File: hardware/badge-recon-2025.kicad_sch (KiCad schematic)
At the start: 72 parts, among them J3 Battery, J5 OLED, P1 USB_C_Plug_USB2.0, Q1 DMG3415U-7, SW1 SW_Push, SW2 SW_Push, SW3 ON, SW4 SOURCE MAG, SW5 SW_Push, SW6 SW_Push, SW7 RESET, SW8 SW_Push, U1 PN7150B0HN_C11002E-PN7150B0HN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, U2 RP2040, U3 AP2114H, U4 W25Q16JV, U5 TC4424, Y1 27.12Mhz, Y2 12Mhz

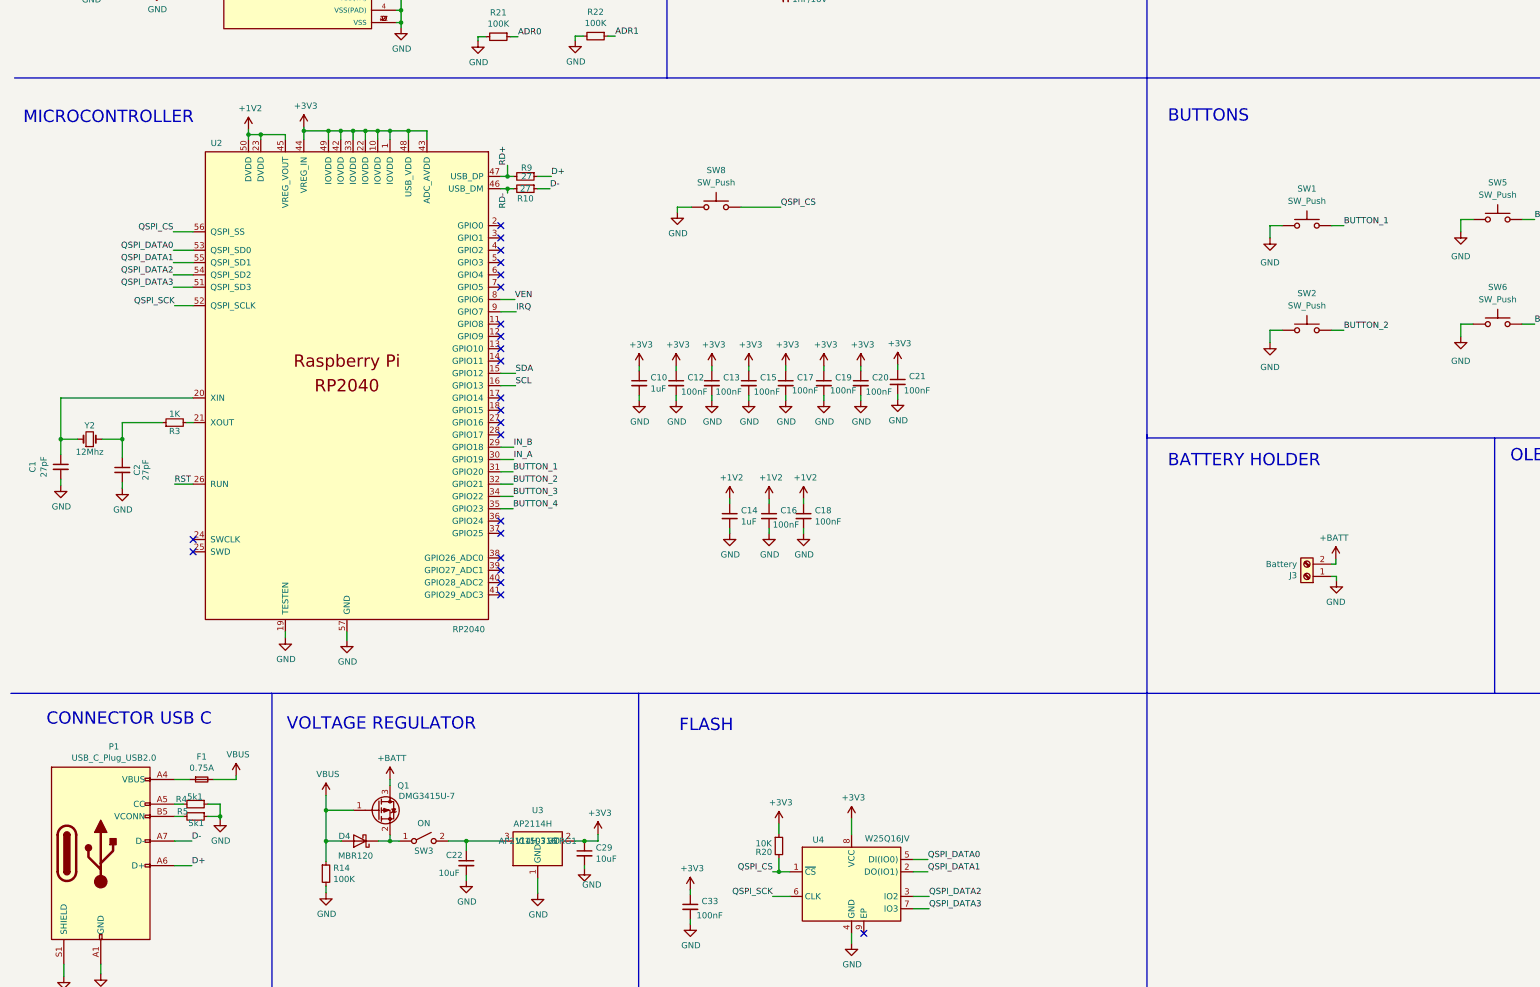
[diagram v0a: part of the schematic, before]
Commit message: feat(Hw): add expansor, 0 unconnected, missing pn7150 crystal
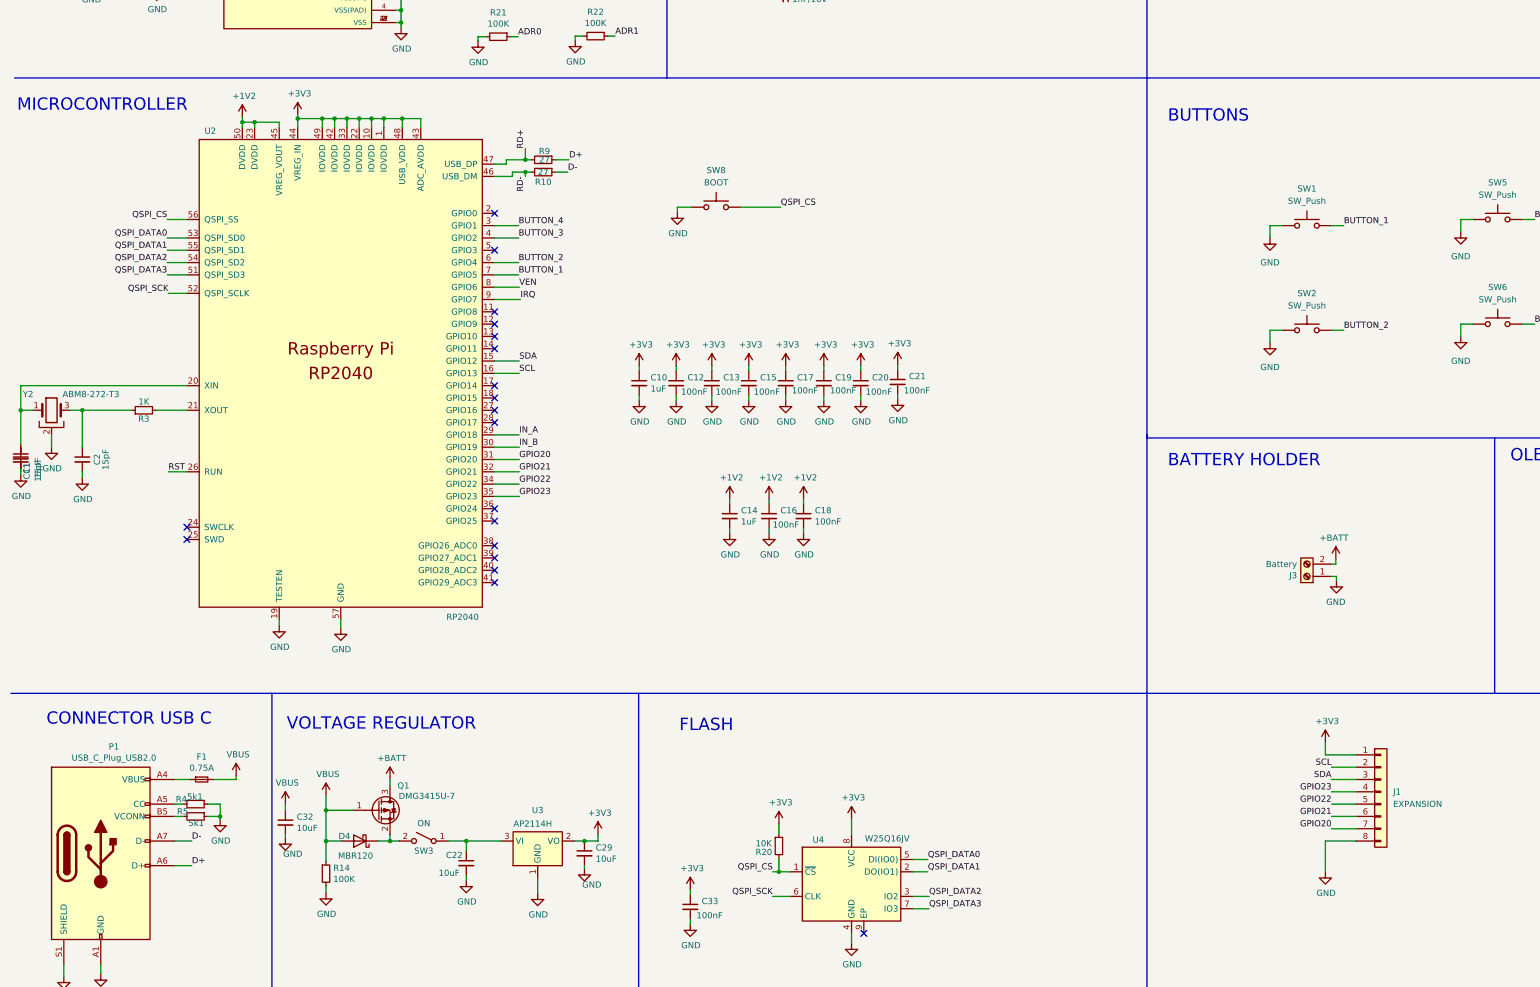
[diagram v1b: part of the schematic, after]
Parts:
- removed Y2: 12Mhz, Crystal:Crystal_SMD_5032-2Pin_5.0x3.2mm, symbol Device:Crystal_Small
- added C11: 15pF, Capacitor_SMD:C_0603_1608Metric, symbol Device:C_Small
- added C32: 10uF, Capacitor_SMD:C_0603_1608Metric, symbol Device:C_Small
- added J1: EXPANSION, Connector_PinHeader_2.54mm:PinHeader_1x08_P2.54mm_Vertical, symbol Connector_Generic:Conn_01x08
- added Y2: ABM8-272-T3, Crystal:Crystal_SMD_Abracon_ABM8G-4Pin_3.2x2.5mm, symbol Device:Crystal_GND2
- C1, C2: value 27pF -> 15pF; LCSC# C92670 -> C1644
- SW8: value SW_Push -> BOOT
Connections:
- net +3V3: now also J1.1 (Pin_1)
- net BUTTON_1: now also U2.7 (GPIO5); no longer U2.31 (GPIO20)
- net BUTTON_2: now also U2.6 (GPIO4); no longer U2.32 (GPIO21)
- net BUTTON_3: now also U2.4 (GPIO2); no longer U2.34 (GPIO22)
- net BUTTON_4: now also U2.3 (GPIO1); no longer U2.35 (GPIO23)
- net GND: now also C32.2, J1.8 (Pin_8), Y2.2
- net IN_A: now also U2.29 (GPIO18); no longer U2.30 (GPIO19)
- net IN_B: now also U2.30 (GPIO19); no longer U2.29 (GPIO18)
- net SCL: now also J1.2 (Pin_2)
- net SDA: now also J1.3 (Pin_3)
- net VBUS: now also C32.1
- net at C1.1, U2.20 (XIN): now also Y2.1
- net at C2.1, R3.1: now also Y2.3
- net at D4.1 (K), Q1.2 (S): now also SW3.2 (B); no longer SW3.1 (A)
- net at C22.1, U3.3 (VI): now also SW3.1 (A); no longer SW3.2 (B)
- new net GPIO20: J1.7 (Pin_7), U2.31 (GPIO20)
- new net GPIO21: J1.6 (Pin_6), U2.32 (GPIO21)
- new net GPIO22: J1.5 (Pin_5), U2.34 (GPIO22)
- new net GPIO23: J1.4 (Pin_4), U2.35 (GPIO23)
- no-connect marks 26 -> 22
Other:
- moved on the sheet: C1, C2, R10, R3, R9, U2

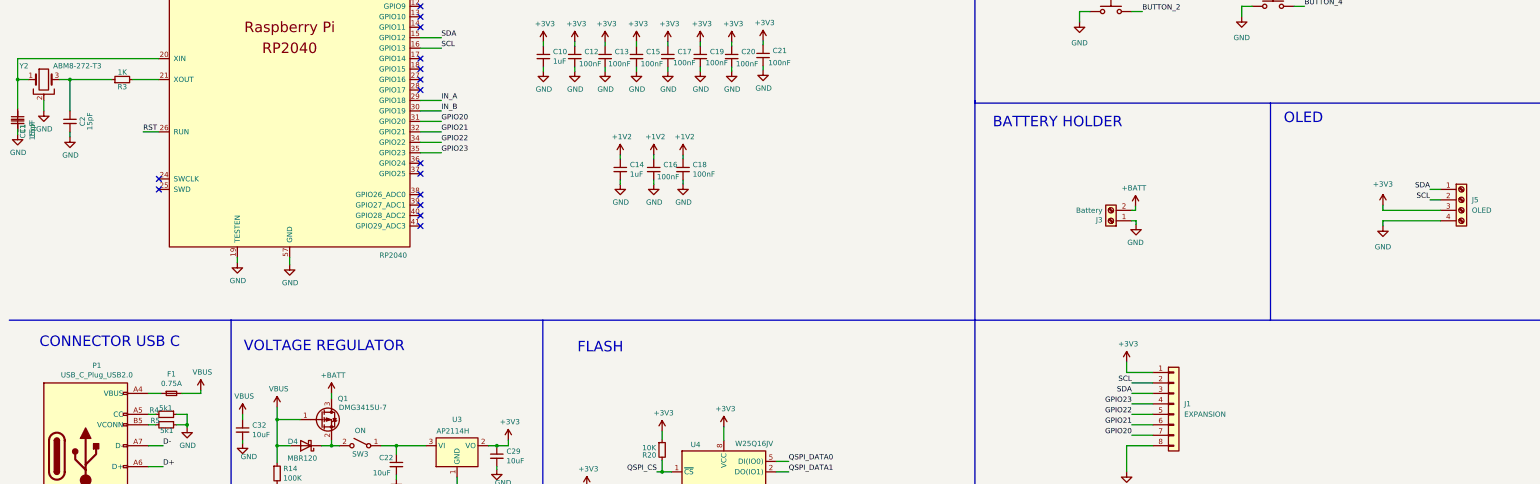
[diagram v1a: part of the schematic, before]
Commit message: feat(Hw): update part numbers for jlcpcb
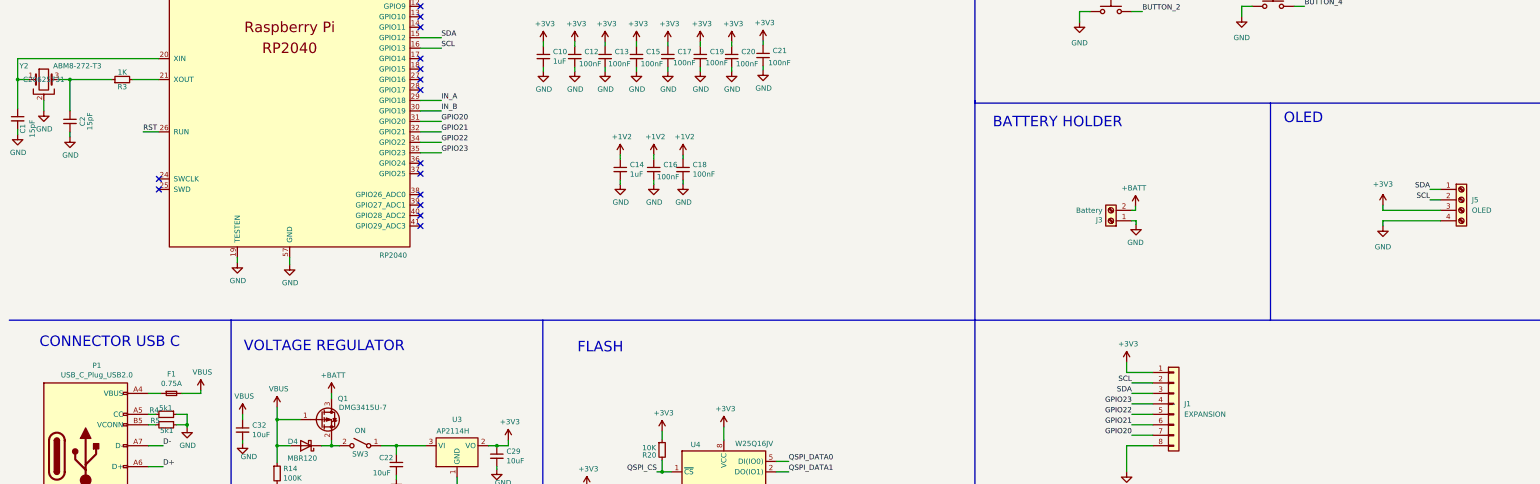
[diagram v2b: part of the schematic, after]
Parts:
- removed C11: 15pF, Capacitor_SMD:C_0603_1608Metric, symbol Device:C_Small
- J1, J5: LCSC# (none) -> -
- U5: manf# TC4424AVOA -> C7498963
- Y1: LCSC# C910048 -> C338245; manf# 520-271.2-6-37-JTNT -> XRCGB27M120F3M10R0
- Y2: LCSC# (none) -> C20625731
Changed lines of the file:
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@@
 			)
 		)
+		(property "LCSC#" "-"
+			(at 294.64 238.76 0)
+			(effects
+				(font
+					(size 1.27 1.27)
+				)
+			)
+		)
 		(pin "3"
 		)
@@
 			)
 		)
-		(property "manf#" "520-271.2-6-37-JTNT"
+		(property "manf#" "XRCGB27M120F3M10R0"
 			(at 28.575 63.627 0)
 			(effects
@@
 			)
 		)
-		(property "LCSC#" "C910048"
+		(property "LCSC#" "C338245"
 			(at 28.575 63.627 0)
 			(effects
@@
 			)
 		)
+		(property "LCSC#" "-"
+			(at 364.49 189.23 0)
+			(effects
+				(font
+					(size 1.27 1.27)
+				)
+			)
+		)
 		(pin "1"
 		)
@@
 			)
 		)
-		(property "manf#" "TC4424AVOA"
+		(property "manf#" "C7498963"
 			(at 327.787 45.339 0)
 			(effects
@@
 			)
 		)
+		(property "LCSC#" "C20625731 "
+			(at 20.32 160.02 0)
+			(effects
+				(font
+					(size 1.27 1.27)
+				)
+			)
+		)
 		(pin "1"
 		)
@@
 					(unit 1)
 				)
-			)
-		)
-	)
-	(symbol
-		(lib_id "Device:C_Small")
-		(at 13.97 170.18 0)
-		(unit 1)
-		(exclude_from_sim no)
-		(in_bom yes)
-		(on_board yes)
-		(dnp no)
-		(property "Reference" "C11"
-			(at 15.2146 172.593 90)
-			(effects
-				(font
-					(size 1.27 1.27)
-				)
-			)
-		)
-		(property "Value" "15pF"
-			(at 17.526 172.593 90)
-			(effects
-				(font
-					(size 1.27 1.27)
-				)
-			)
-		)
-		(property "Footprint" "Capacitor_SMD:C_0603_1608Metric"
-			(at 13.97 170.18 0)
-			(effects
-				(font
-					(size 1.27 1.27)
-				)
-				(hide yes)
-			)
-		)
-		(property "Datasheet" ""
-			(at 13.97 170.18 0)
-			(effects
-				(font
-					(size 1.27 1.27)
-				)
-				(hide yes)
-			)
-		)
-		(property "Description" ""
-			(at 13.97 170.18 0)
-			(effects
-				(font
-					(size 1.27 1.27)
-				)
-			)
-		)
-		(property "LCSC#" "C1644"
-			(at 13.97 170.18 0)
-			(effects
-				(font
-					(size 1.27 1.27)
-				)
-				(hide yes)
-			)
-		)
-		(property "manf#" ""
-			(at 13.97 170.18 0)
-			(effects
-				(font
-					(size 1.27 1.27)
-				)
-				(hide yes)
-			)
-		)
-		(property "provedor" "LCSC"
-			(at 13.97 170.18 0)
-			(effects
-				(font
-					(size 1.27 1.27)
-				)
-				(hide yes)
-			)
-		)
-		(pin "1"
-		)
-		(pin "2"
-		)
-		(instances
-			(project "badge-recon-2025"
-				(path "/d927dcf1-a70e-4351-8ddc-20f742435b21"
-					(reference "C11")
-					(unit 1)
-				)

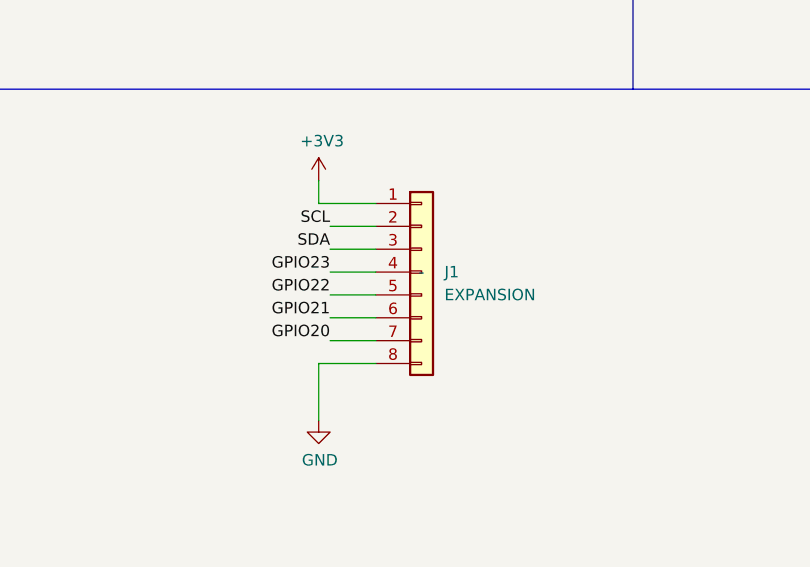
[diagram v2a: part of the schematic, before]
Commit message: fix(Hw): set component as dnp & move routes
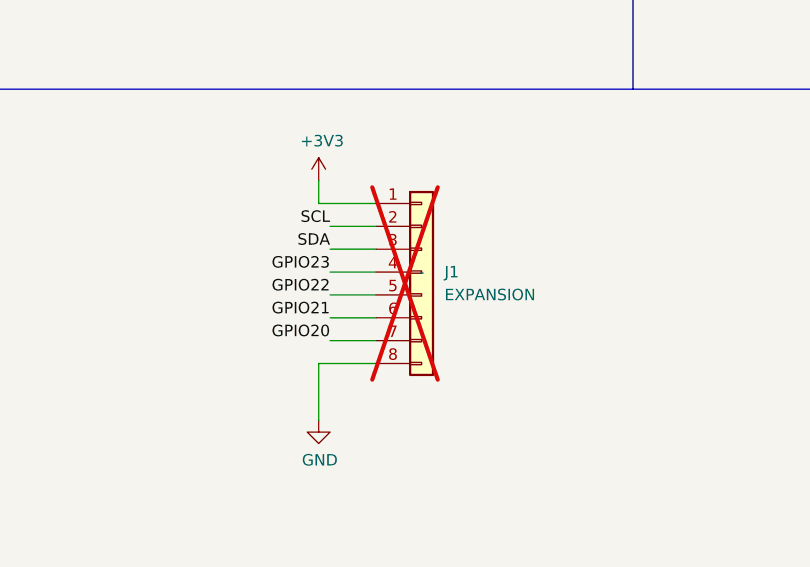
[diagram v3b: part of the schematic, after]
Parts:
- J1: now not fitted
- U5: LCSC# TC4424AVOA -> C7498963; manf# C7498963 -> TC4424AVOA
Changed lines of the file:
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@@
 		(in_bom yes)
 		(on_board yes)
-		(dnp no)
+		(dnp yes)
 		(fields_autoplaced yes)
 		(property "Reference" "J1"
@@
 			)
 		)
-		(property "LCSC#" "TC4424AVOA"
+		(property "LCSC#" "C7498963"
 			(at 327.787 45.339 0)
 			(effects
@@
 			)
 		)
-		(property "manf#" "C7498963"
+		(property "manf#" "TC4424AVOA"
 			(at 327.787 45.339 0)
 			(effects
